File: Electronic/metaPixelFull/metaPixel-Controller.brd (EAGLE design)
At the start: 81.3 x 68.6 mm, 18 parts, among them IC1 MAX481CPA, IC2 TEENSY_3.1, IC3 74HCT245N, J1 PWR

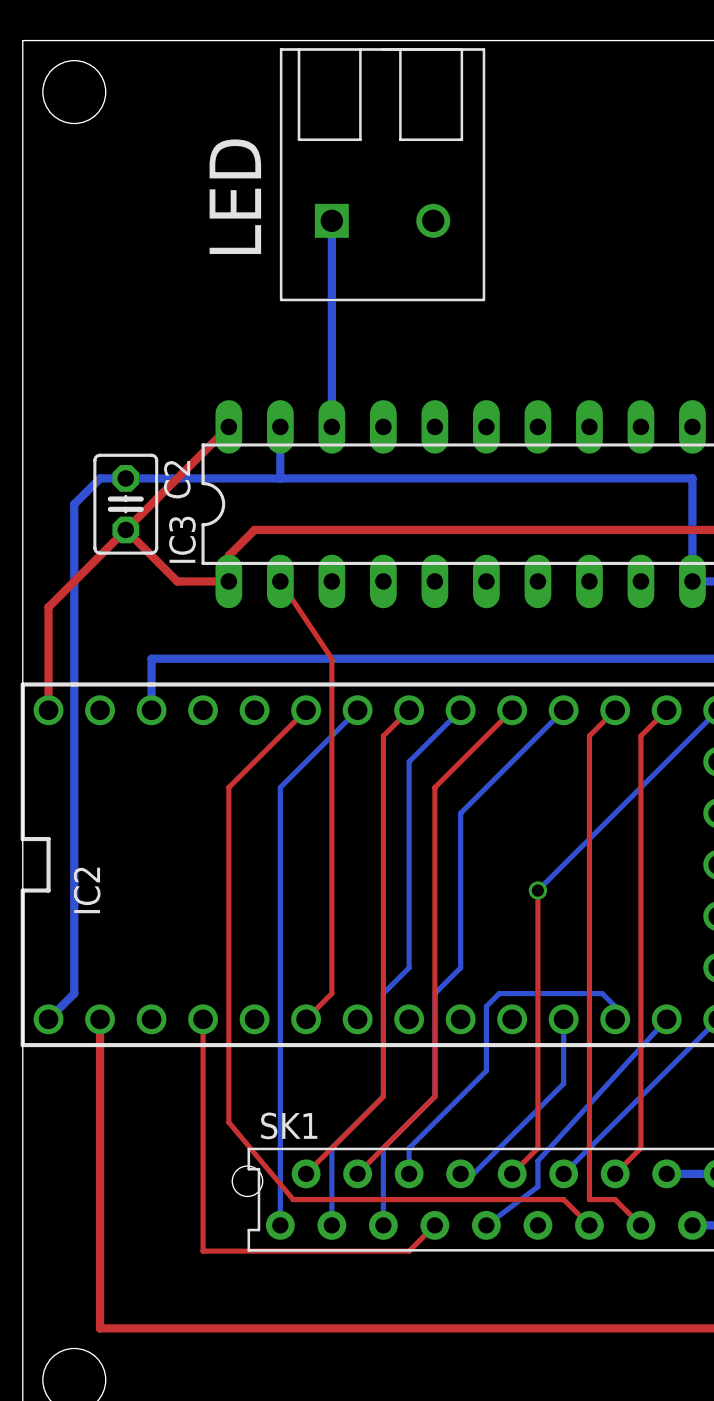
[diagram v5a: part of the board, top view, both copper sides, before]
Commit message: added some warning if module dimensions are not set
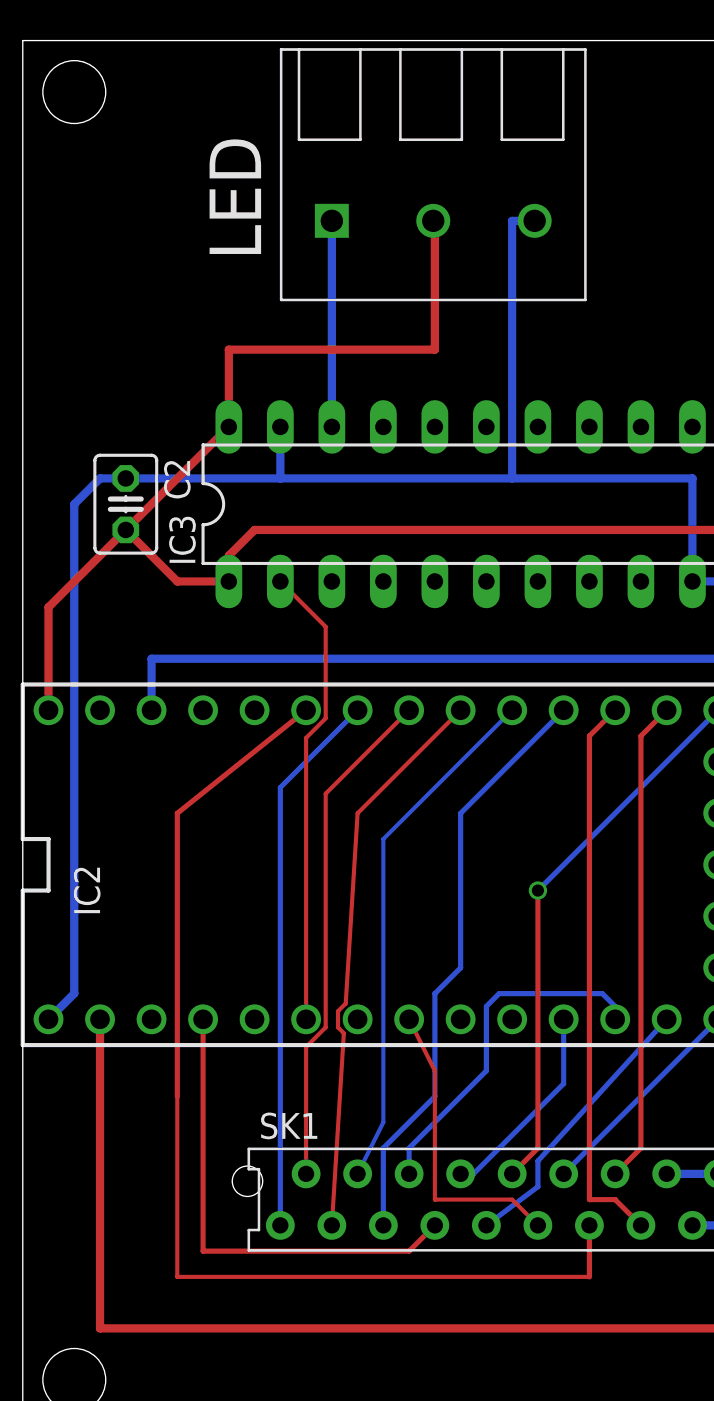
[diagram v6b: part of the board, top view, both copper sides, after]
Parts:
- LED: value RP025-02 -> RP025-03; device RP025xx:RP025-02 -> RP025xx:RP025-03
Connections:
- net GND: now also LED.P$3
- net VCC: now also LED.P$2
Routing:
- net VCC: track 126.1 -> 146.4 mm
- net LCD_LED: track 0.00 -> 14.8 mm
- net GND: track 169.2 -> 183.0 mm
- net !MEM_CS: track 42.0 -> 53.9 mm
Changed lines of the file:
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@@
 <?xml version="1.0" encoding="utf-8"?>
 <!DOCTYPE eagle SYSTEM "eagle.dtd">
-<eagle version="7.5.0">
+<eagle version="8.3.1">
 <drawing>
 <settings>
 <setting alwaysvectorfont="yes"/>
+<setting keepoldvectorfont="yes"/>
 <setting verticaltext="up"/>
 </settings>
@@
 <element name="C2" library="resistor" package="C025-030X050" value="0.1µ" x="5.08" y="45.72" rot="R270"/>
 <element name="DC1" library="dc-dc-converter" package="NME" value="NME0505" x="62.23" y="24.13" rot="R180">
+<attribute name="MF" value="C &amp; D TECHNOLOGIES, INC" x="62.23" y="24.13" size="1.778" layer="27" rot="R180" display="off"/>
+<attribute name="MPN" value="NME1205D" x="62.23" y="24.13" size="1.778" layer="27" rot="R180" display="off"/>
+<attribute name="OC_FARNELL" value="1021466" x="62.23" y="24.13" size="1.778" layer="27" rot="R180" display="off"/>
 <attribute name="OC_NEWARK" value="98B8198" x="62.23" y="24.13" size="1.778" layer="27" rot="R180" display="off"/>
-<attribute name="MF" value="C &amp; D TECHNOLOGIES, INC" x="62.23" y="24.13" size="1.778" layer="27" rot="R180" display="off"/>
-<attribute name="OC_FARNELL" value="1021466" x="62.23" y="24.13" size="1.778" layer="27" rot="R180" display="off"/>
-<attribute name="MPN" value="NME1205D" x="62.23" y="24.13" size="1.778" layer="27" rot="R180" display="off"/>
 </element>
 <element name="DMX_1" library="RP025xx" package="RP025-03" value="RP025-03" x="72.39" y="44.69" smashed="yes" rot="R270">
@@
 </element>
 <element name="IC1" library="maxim" package="DIL08" value="MAX481CPA" x="52.07" y="39.37" rot="R270">
+<attribute name="MF" value="" x="52.07" y="39.37" size="1.778" layer="27" rot="R270" display="off"/>
+<attribute name="MPN" value="MAX481CPA+" x="52.07" y="39.37" size="1.778" layer="27" rot="R270" display="off"/>
+<attribute name="OC_FARNELL" value="unknown" x="52.07" y="39.37" size="1.778" layer="27" rot="R270" display="off"/>
 <attribute name="OC_NEWARK" value="99K3445" x="52.07" y="39.37" size="1.778" layer="27" rot="R270" display="off"/>
-<attribute name="MF" value="" x="52.07" y="39.37" size="1.778" layer="27" rot="R270" display="off"/>
-<attribute name="OC_FARNELL" value="unknown" x="52.07" y="39.37" size="1.778" layer="27" rot="R270" display="off"/>
-<attribute name="MPN" value="MAX481CPA+" x="52.07" y="39.37" size="1.778" layer="27" rot="R270" display="off"/>
 </element>
 <element name="IC3" library="74xx-eu" package="DIL20" value="74HCT245N" x="21.59" y="45.72"/>
-<element name="LED" library="RP025xx" package="RP025-02" value="RP025-02" x="15.24" y="59.69" smashed="yes">
+<element name="LED" library="RP025xx" package="RP025-03" value="RP025-03" x="15.24" y="59.69" smashed="yes">
 <attribute name="NAME" x="11.75" y="60.82" size="2.54" layer="21" rot="R90" align="bottom-center"/>
 </element>
 <element name="OK1" library="optocoupler" package="DIL08" value="6N137" x="49.53" y="25.4" rot="R180">
+<attribute name="MF" value="" x="49.53" y="25.4" size="1.778" layer="27" rot="R180" display="off"/>
+<attribute name="MPN" value="6N137" x="49.53" y="25.4" size="1.778" layer="27" rot="R180" display="off"/>
+<attribute name="OC_FARNELL" value="1328376" x="49.53" y="25.4" size="1.778" layer="27" rot="R180" display="off"/>
 <attribute name="OC_NEWARK" value="52M1895" x="49.53" y="25.4" size="1.778" layer="27" rot="R180" display="off"/>
-<attribute name="MF" value="" x="49.53" y="25.4" size="1.778" layer="27" rot="R180" display="off"/>
-<attribute name="OC_FARNELL" value="1328376" x="49.53" y="25.4" size="1.778" layer="27" rot="R180" display="off"/>
-<attribute name="MPN" value="6N137" x="49.53" y="25.4" size="1.778" layer="27" rot="R180" display="off"/>
 </element>
 <element name="PWR" library="RP025xx" package="RP025-02" value="RP025-02" x="72.39" y="25.96" smashed="yes" rot="R270">
@@
 <wire x1="38.1" y1="27.94" x2="38.1" y2="24.13" width="0.4064" layer="16"/>
 <wire x1="38.1" y1="24.13" x2="45.72" y2="24.13" width="0.4064" layer="16"/>
+<contactref element="LED" pad="P$3"/>
+<wire x1="24.13" y1="46.99" x2="24.13" y2="59.69" width="0.4064" layer="16"/>
+<wire x1="24.13" y1="59.69" x2="25.24" y2="59.69" width="0.4064" layer="16"/>
+<wire x1="33.02" y1="46.99" x2="24.13" y2="46.99" width="0" layer="19" extent="16-16"/>
 </signal>
 <signal name="VCC" class="1">
@@
 <wire x1="10.16" y1="41.91" x2="7.62" y2="41.91" width="0.4064" layer="1"/>
 <wire x1="7.62" y1="41.91" x2="5.08" y2="44.45" width="0.4064" layer="1"/>
-<wire x1="10.16" y1="49.53" x2="5.08" y2="44.45" width="0.4064" layer="1"/>
+<wire x1="5.08" y1="44.45" x2="10.16" y2="49.53" width="0.4064" layer="1"/>
 <wire x1="10.16" y1="41.91" x2="10.16" y2="43.18" width="0.4064" layer="1"/>
 <wire x1="10.16" y1="43.18" x2="11.43" y2="44.45" width="0.4064" layer="1"/>
@@
 <wire x1="67.35" y1="13.8" x2="66.04" y2="13.97" width="0.4064" layer="1"/>
 <wire x1="66.04" y1="13.97" x2="66.04" y2="15.24" width="0.4064" layer="1"/>
+<contactref element="LED" pad="P$2"/>
+<wire x1="10.16" y1="49.53" x2="10.16" y2="53.34" width="0.4064" layer="1"/>
+<wire x1="10.16" y1="53.34" x2="20.32" y2="53.34" width="0.4064" layer="1"/>
+<wire x1="20.32" y1="53.34" x2="20.32" y2="59.61" width="0.4064" layer="1"/>
+<wire x1="20.32" y1="59.61" x2="20.24" y2="59.69" width="0.1524" layer="1"/>
 </signal>
 <signal name="LED_OUT" class="1">
@@
 <contactref element="IC3" pad="2"/>
 <contactref element="IC2" pad="4"/>
-<wire x1="13.97" y1="20.32" x2="15.24" y2="21.59" width="0.254" layer="1"/>
-<wire x1="15.24" y1="21.59" x2="15.24" y2="38.1" width="0.254" layer="1"/>
-<wire x1="15.24" y1="38.1" x2="12.7" y2="41.91" width="0.254" layer="1"/>
+<wire x1="13.97" y1="20.32" x2="13.97" y2="34.195" width="0.2032" layer="1"/>
+<wire x1="13.97" y1="34.195" x2="14.9352" y2="35.1602" width="0.2032" layer="1"/>
+<wire x1="14.9352" y1="35.1602" x2="14.9352" y2="39.6748" width="0.2032" layer="1"/>
+<wire x1="14.9352" y1="39.6748" x2="12.7" y2="41.91" width="0.2032" layer="1"/>
 </signal>
 <signal name="GND_EXT" class="1">
@@
 <contactref element="SK1" pad="11"/>
 <contactref element="IC2" pad="6"/>
-<wire x1="25.4" y1="10.16" x2="19.05" y2="20.32" width="0" layer="19" extent="1-1"/>
+<wire x1="25.4" y1="10.16" x2="24.13" y2="11.43" width="0.2032" layer="1"/>
+<wire x1="24.13" y1="11.43" x2="20.32" y2="11.43" width="0.2032" layer="1"/>
+<wire x1="20.32" y1="11.43" x2="20.32" y2="17.78" width="0.2032" layer="1"/>
+<wire x1="20.32" y1="17.78" x2="19.05" y2="20.32" width="0.2032" layer="1"/>
 </signal>
 <signal name="KEY_1">
@@
 <contactref element="SK1" pad="2"/>
 <contactref element="IC2" pad="19/A5"/>
-<wire x1="17.78" y1="16.51" x2="13.97" y2="12.7" width="0.254" layer="1"/>
-<wire x1="17.78" y1="34.29" x2="17.78" y2="16.51" width="0.254" layer="1"/>
-<wire x1="19.05" y1="35.56" x2="17.78" y2="34.29" width="0.254" layer="1"/>
+<wire x1="13.97" y1="12.7" x2="13.97" y2="18.955" width="0.2032" layer="1"/>
+<wire x1="13.97" y1="18.955" x2="14.9352" y2="19.9202" width="0.2032" layer="1"/>
+<wire x1="14.9352" y1="31.4452" x2="19.05" y2="35.56" width="0.2032" layer="1"/>
+<wire x1="14.9352" y1="19.9202" x2="14.9352" y2="31.4452" width="0.2032" layer="1"/>
 </signal>
 <signal name="KEY_3">
 <contactref element="SK1" pad="3"/>
 <contactref element="IC2" pad="18/A4"/>
-<wire x1="21.59" y1="35.56" x2="19.05" y2="33.02" width="0.254" layer="16"/>
-<wire x1="19.05" y1="33.02" x2="19.05" y2="22.86" width="0.254" layer="16"/>
-<wire x1="19.05" y1="22.86" x2="17.78" y2="21.59" width="0.254" layer="16"/>
-<wire x1="17.78" y1="21.59" x2="17.78" y2="16.51" width="0.254" layer="16"/>
-<wire x1="17.78" y1="16.51" x2="15.24" y2="13.97" width="0.254" layer="16"/>
-<wire x1="15.24" y1="13.97" x2="15.24" y2="10.16" width="0.254" layer="16"/>
+<wire x1="21.59" y1="35.56" x2="16.51" y2="30.48" width="0.2032" layer="1"/>
+<wire x1="16.51" y1="30.48" x2="15.923665625" y2="21.098665625" width="0.2032" layer="1"/>
+<wire x1="15.923665625" y1="21.098665625" x2="15.5448" y2="20.7198" width="0.2032" layer="1"/>
+<wire x1="15.5448" y1="20.7198" x2="15.5448" y2="19.9202" width="0.2032" layer="1"/>
+<wire x1="15.5448" y1="19.9202" x2="15.832059375" y2="19.632940625" width="0.2032" layer="1"/>
+<wire x1="15.832059375" y1="19.632940625" x2="15.24" y2="10.16" width="0.2032" layer="1"/>
 </signal>
 <signal name="KEY_4">
 <contactref element="IC2" pad="17/A3"/>
 <contactref element="SK1" pad="4"/>
-<wire x1="20.32" y1="16.51" x2="16.51" y2="12.7" width="0.254" layer="1"/>
-<wire x1="20.32" y1="31.75" x2="20.32" y2="16.51" width="0.254" layer="1"/>
-<wire x1="24.13" y1="35.56" x2="20.32" y2="31.75" width="0.254" layer="1"/>
+<wire x1="17.78" y1="29.21" x2="17.78" y2="15.24" width="0.2032" layer="16"/>
+<wire x1="17.78" y1="15.24" x2="16.51" y2="12.7" width="0.2032" layer="16"/>
+<wire x1="24.13" y1="35.56" x2="17.78" y2="29.21" width="0.2032" layer="16"/>
 </signal>
 <signal name="KEY_5">
@@
 <contactref element="SK1" pad="13"/>
 <contactref element="IC2" pad="21/A7"/>
-<wire x1="27.94" y1="10.16" x2="26.67" y2="11.43" width="0.254" layer="1"/>
-<wire x1="26.67" y1="11.43" x2="13.335" y2="11.43" width="0.254" layer="1"/>
-<wire x1="13.335" y1="11.43" x2="10.16" y2="15.24" width="0.254" layer="1"/>
-<wire x1="10.16" y1="15.24" x2="10.16" y2="31.75" width="0.254" layer="1"/>
-<wire x1="10.16" y1="31.75" x2="13.97" y2="35.56" width="0.254" layer="1"/>
+<wire x1="27.94" y1="10.16" x2="27.94" y2="7.62" width="0.254" layer="1"/>
+<wire x1="7.62" y1="16.51" x2="7.62" y2="30.48" width="0.254" layer="1"/>
+<wire x1="7.62" y1="30.48" x2="13.97" y2="35.56" width="0.254" layer="1"/>
+<wire x1="27.94" y1="7.62" x2="7.62" y2="7.62" width="0.2032" layer="1"/>
+<wire x1="7.62" y1="7.62" x2="7.62" y2="16.51" width="0.2032" layer="1"/>
 </signal>
 <signal name="ENC_A">
